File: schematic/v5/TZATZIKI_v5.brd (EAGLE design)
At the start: 41.1 x 50.1 mm, 21 parts, among them J1 2X20-CHIP-HEADERS2X20CHIP_OFF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, U2 DS2431P

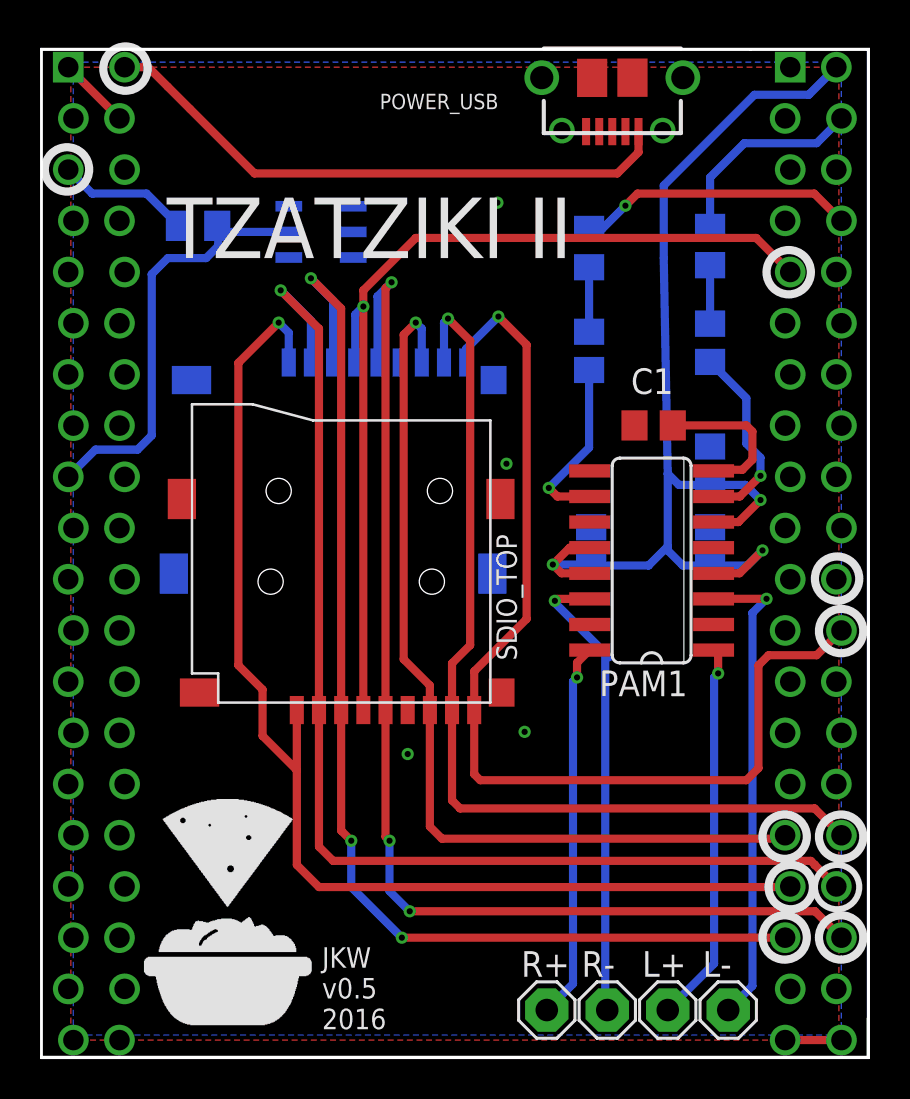
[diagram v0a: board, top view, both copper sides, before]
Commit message: connected audio gnd
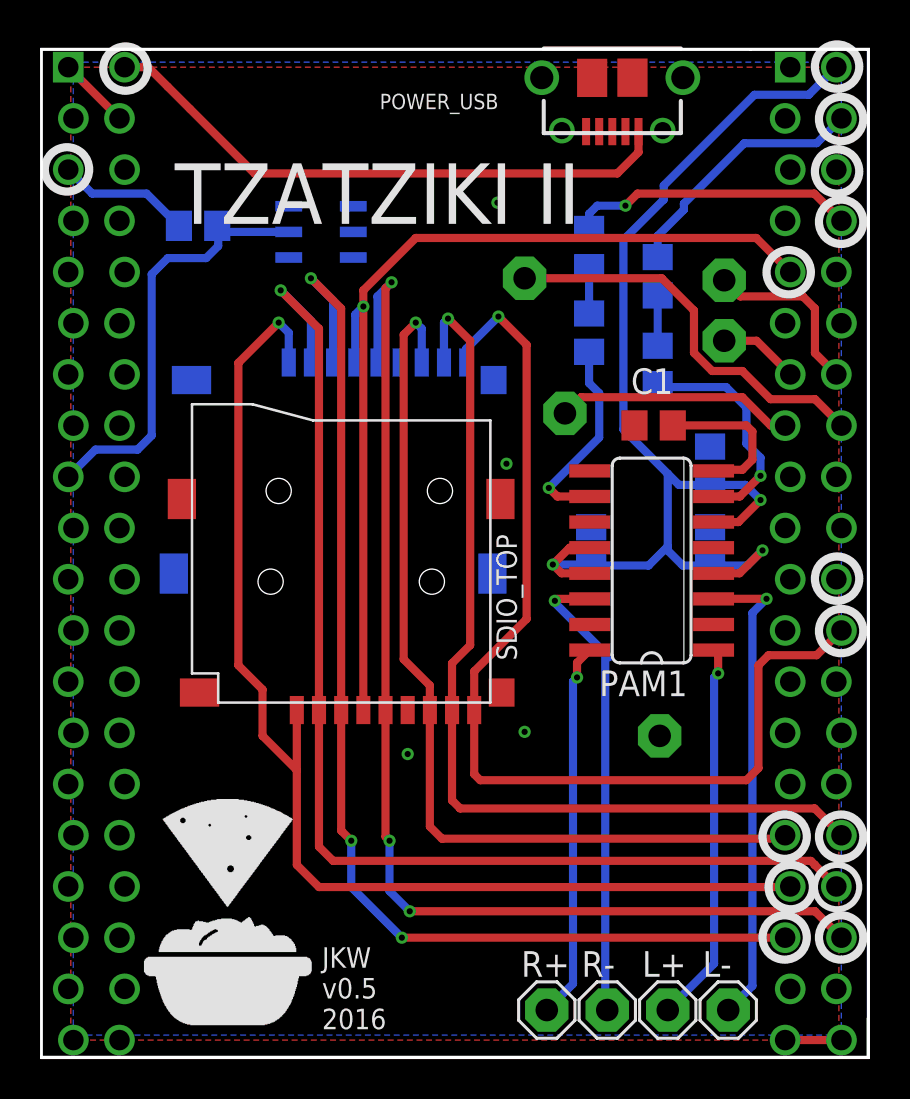
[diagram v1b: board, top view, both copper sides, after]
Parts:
- added GND, P0, P1, P3, P4: SE11, solpad:SE11
- moved R1 3.00 mm to (38.0, 54.4)
- moved C5 2.82 mm to (38.0, 50.0)
- moved C4 0.90 mm to (34.6, 51.6)
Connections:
- new net N$23: J1.XIO-P1, P1.MP
- new net N$24: J1.XIO-P3, P3.MP
- new net N$25: J1.XIO-P0, P0.MP
- new net N$26: J1.XIO-P2, P4.MP
- net GND: now also GND.MP, J1.HPCOM
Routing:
- net N$24: track 0.00 -> 20.0 mm
- net N$26: track 0.00 -> 11.8 mm
- net N$23: track 0.00 -> 8.79 mm
- net N$25: track 0.00 -> 3.97 mm
- net N$19: track 10.2 -> 12.8 mm
- net N$15: track 9.44 -> 11.3 mm
- net N$7: track 55.5 -> 57.3 mm
- net N$18: track 8.88 -> 10.2 mm
- net N$21: track 3.20 -> 2.30 mm

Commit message: added shutdown pin control
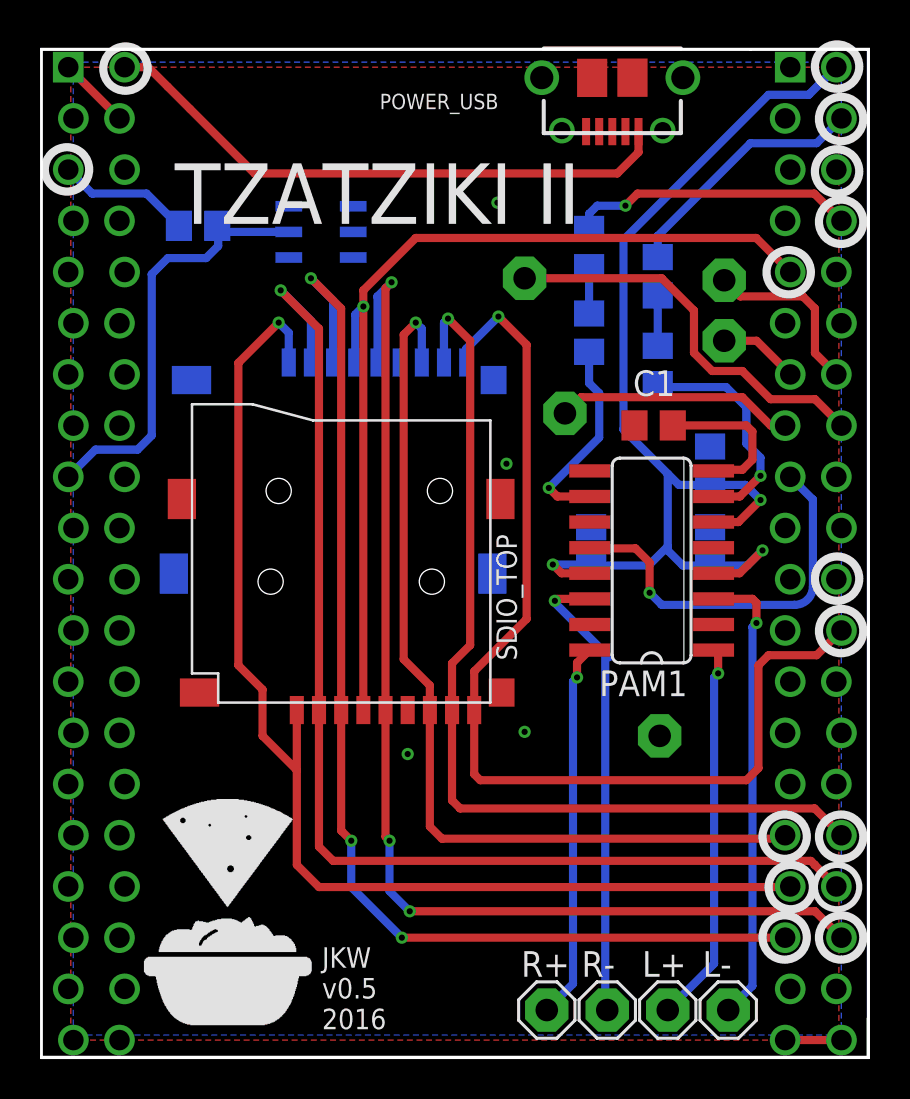
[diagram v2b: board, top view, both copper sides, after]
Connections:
- new net N$27: J1.XIO-P4, PAM1.12
- net N$7: no longer PAM1.12
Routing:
- net N$27: track 0.00 -> 19.4 mm, vias 0 -> 1
- net N$7: track 57.3 -> 54.7 mm
- net N$12: track 23.8 -> 23.0 mm

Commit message: added bat con and pwrbutton
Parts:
- added PWR-BTN, VBAT: (no value), pinhead:1X02
- moved U$2 8.99 mm to (31.6, 19.5)
- moved U$1 7.83 mm to (20.3, 17.9)
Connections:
- new net N$28: J1.BAT, VBAT.2
- new net N$29: J1.PWRON, PWR-BTN.2
- net GND: now also PWR-BTN.1, VBAT.1
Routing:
- net N$28: track 0.00 -> 38.5 mm
- net N$29: track 0.00 -> 27.7 mm
- net N$11: track 19.0 -> 21.9 mm
- net N$13: track 18.7 -> 19.5 mm
- net GND: vias 4 -> 5

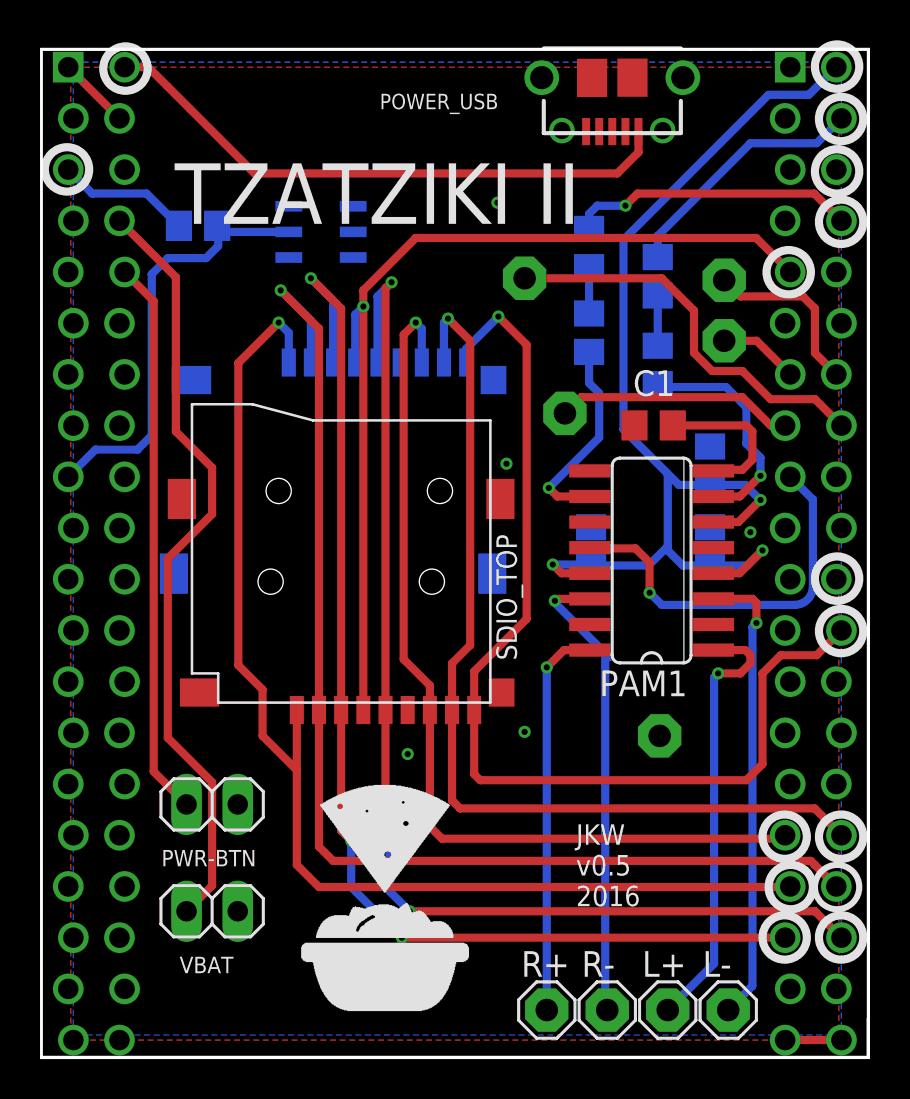
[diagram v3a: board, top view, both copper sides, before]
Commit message: added bat con and pwrbutton
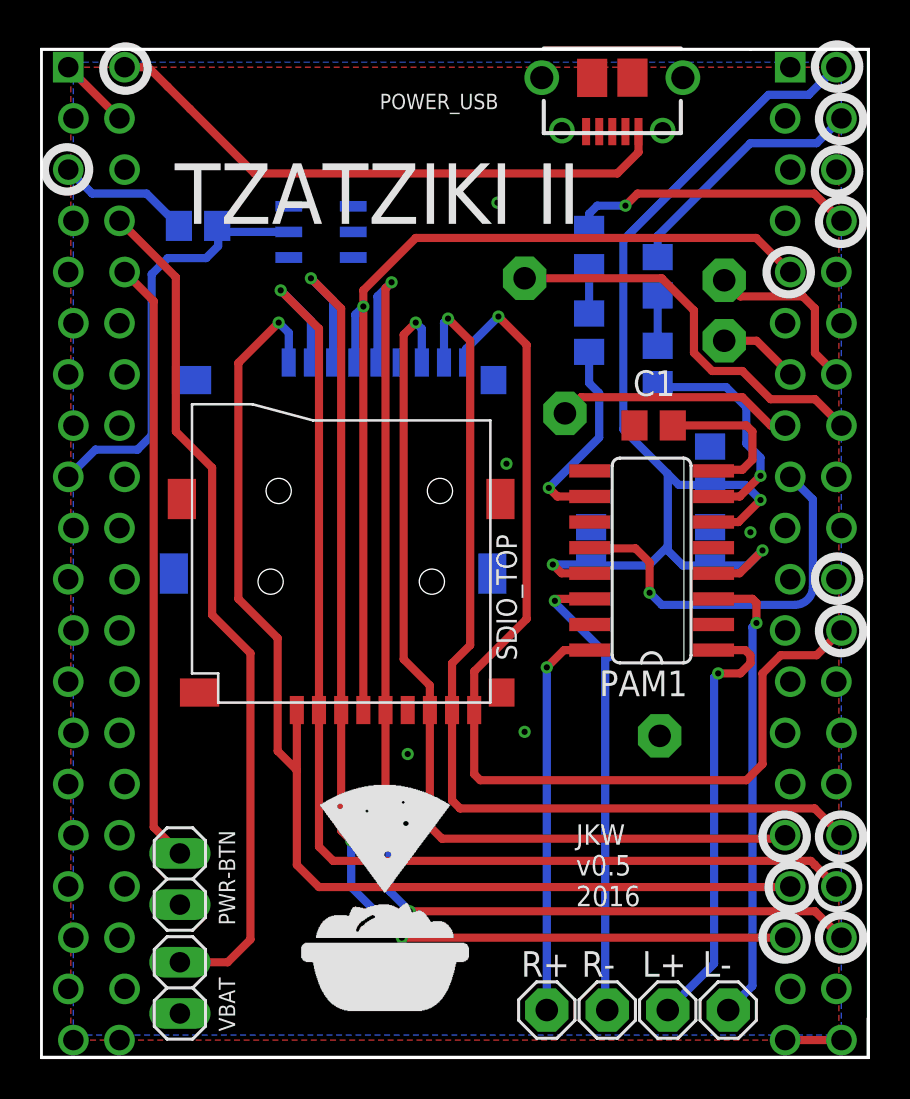
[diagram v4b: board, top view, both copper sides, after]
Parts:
- moved VBAT 4.12 mm to (14.3, 19.1), turned to 90 degrees
- moved PWR-BTN 4.03 mm to (14.3, 24.5), turned to 90 degrees
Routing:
- net N$28: track 38.5 -> 42.3 mm
- net N$29: track 27.7 -> 30.0 mm
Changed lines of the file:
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@@
 <element name="P4" library="solpad" package="SE11" value="SE11" x="33.4" y="47.6" rot="MR180"/>
 <element name="GND" library="solpad" package="SE11" value="SE11" x="38.1" y="31.6" rot="MR180"/>
-<element name="PWR-BTN" library="pinhead" package="1X02" value="" x="15.9" y="28.2" smashed="yes" rot="R180">
-<attribute name="NAME" x="13.3838" y="25.1288" size="0.8128" layer="25" ratio="10"/>
-<attribute name="VALUE" x="18.44" y="31.375" size="1.27" layer="27" rot="R180"/>
+<element name="PWR-BTN" library="pinhead" package="1X02" value="" x="14.3" y="24.5" smashed="yes" rot="R90">
+<attribute name="NAME" x="16.2288" y="26.9162" size="0.8128" layer="25" ratio="10" rot="R270"/>
+<attribute name="VALUE" x="17.475" y="21.96" size="1.27" layer="27" rot="R90"/>
 </element>
-<element name="VBAT" library="pinhead" package="1X02" value="" x="15.9" y="22.9" smashed="yes" rot="R180">
-<attribute name="NAME" x="14.2838" y="19.8288" size="0.8128" layer="25" ratio="10"/>
-<attribute name="VALUE" x="18.44" y="26.075" size="1.27" layer="27" rot="R180"/>
+<element name="VBAT" library="pinhead" package="1X02" value="" x="14.3" y="19.1" smashed="yes" rot="R90">
+<attribute name="NAME" x="16.2288" y="19.6162" size="0.8128" layer="25" ratio="10" rot="R270"/>
+<attribute name="VALUE" x="17.475" y="16.56" size="1.27" layer="27" rot="R90"/>
 </element>
 </elements>
@@
 <wire x1="19.2" y1="52.1" x2="19.7" y2="51.6" width="0.4064" layer="16"/>
 <wire x1="19.7" y1="51.6" x2="19.7" y2="50.12" width="0.4064" layer="16"/>
-<wire x1="17.2" y1="35.1" x2="17.2" y2="50.1" width="0.4064" layer="1"/>
 <wire x1="17.2" y1="50.1" x2="19.2" y2="52.1" width="0.4064" layer="1"/>
-<wire x1="17.2" y1="35.1" x2="18.4" y2="33.9" width="0.4064" layer="1"/>
-<wire x1="18.4" y1="33.9" x2="18.4" y2="31.6" width="0.4064" layer="1"/>
-<wire x1="18.4" y1="31.6" x2="20.1" y2="29.9" width="0.4064" layer="1"/>
+<wire x1="19.15" y1="30.85" x2="20.1" y2="29.9" width="0.4064" layer="1"/>
+<wire x1="17.2" y1="50.1" x2="17.2" y2="38.4" width="0.4064" layer="1"/>
+<wire x1="17.2" y1="38.4" x2="19.15" y2="36.45" width="0.4064" layer="1"/>
+<wire x1="19.15" y1="36.45" x2="19.15" y2="30.85" width="0.4064" layer="1"/>
 </signal>
 <signal name="N$5">
@@
 <wire x1="14.1" y1="54.353" x2="14.1" y2="46.7" width="0.4064" layer="1"/>
 <wire x1="14.1" y1="46.7" x2="15.9" y2="44.9" width="0.4064" layer="1"/>
-<wire x1="15.9" y1="44.9" x2="15.9" y2="42.6" width="0.4064" layer="1"/>
-<wire x1="15.9" y1="42.6" x2="13.7" y2="40.4" width="0.4064" layer="1"/>
-<wire x1="13.7" y1="40.4" x2="13.7" y2="31.5" width="0.4064" layer="1"/>
-<wire x1="13.7" y1="31.5" x2="15.9" y2="29.3" width="0.4064" layer="1"/>
-<wire x1="15.9" y1="29.3" x2="15.9" y2="24.17" width="0.4064" layer="1"/>
-<wire x1="15.9" y1="24.17" x2="14.63" y2="22.9" width="0.4064" layer="1"/>
+<wire x1="15.9" y1="44.9" x2="15.9" y2="37.6" width="0.4064" layer="1"/>
+<wire x1="15.9" y1="37.6" x2="17.8" y2="35.7" width="0.4064" layer="1"/>
+<wire x1="17.8" y1="35.7" x2="17.8" y2="21.5" width="0.4064" layer="1"/>
+<wire x1="17.8" y1="21.5" x2="16.67" y2="20.37" width="0.4064" layer="1"/>
+<wire x1="16.67" y1="20.37" x2="14.3" y2="20.37" width="0.4064" layer="1"/>
 </signal>
 <signal name="N$29">
@@
 <contactref element="PWR-BTN" pad="2"/>
 <wire x1="11.557" y1="54.61" x2="13" y2="53.167" width="0.4064" layer="1"/>
-<wire x1="13" y1="53.167" x2="13" y2="29.83" width="0.4064" layer="1"/>
-<wire x1="13" y1="29.83" x2="14.63" y2="28.2" width="0.4064" layer="1"/>
+<wire x1="13" y1="53.167" x2="13" y2="27.07" width="0.4064" layer="1"/>
+<wire x1="13" y1="27.07" x2="14.3" y2="25.77" width="0.4064" layer="1"/>
 </signal>
 </signals>

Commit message: rotated connector for free passage of the SD card
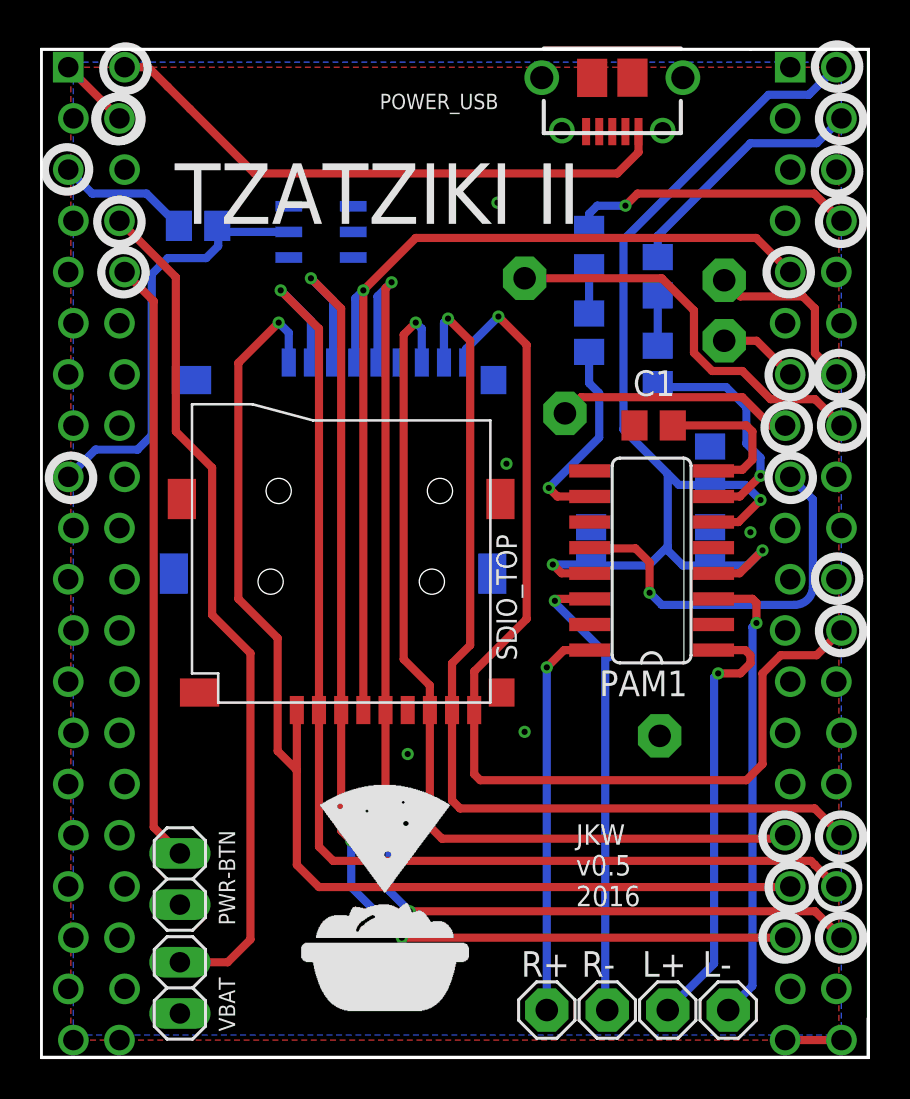
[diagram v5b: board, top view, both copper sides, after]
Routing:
- net N$10: track 46.7 -> 47.5 mm
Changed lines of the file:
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@@
 <circle x="46.9" y="59.7" radius="1.1" width="0.4064" layer="26"/>
 <circle x="46.9" y="59.6" radius="1.1" width="0.4064" layer="25"/>
+<circle x="11.3" y="57.1" radius="1.1" width="0.4064" layer="25"/>
+<circle x="11.5" y="54.6" radius="1.1" width="0.4064" layer="25"/>
+<circle x="8.9" y="44.4" radius="1.1" width="0.4064" layer="25"/>
+<circle x="47.2" y="47" radius="1.1" width="0.4064" layer="25"/>
+<circle x="47" y="49.5" radius="1.1" width="0.4064" layer="25"/>
+<circle x="44.6" y="49.5" radius="1.1" width="0.4064" layer="25"/>
+<circle x="44.4" y="46.9" radius="1.1" width="0.4064" layer="25"/>
+<circle x="44.6" y="44.4" radius="1.1" width="0.4064" layer="25"/>
+<circle x="11.3" y="62.2" radius="1.1" width="0.4064" layer="25"/>
+<circle x="11.2" y="62.2" radius="1.1" width="0.4064" layer="25"/>
+<circle x="11.3" y="62.2" radius="1.1" width="0.4064" layer="26"/>
+<circle x="11.3" y="57.1" radius="1.1" width="0.4064" layer="26"/>
+<circle x="11.6" y="54.6" radius="1.1" width="0.4064" layer="26"/>
+<circle x="8.8" y="44.5" radius="1.1" width="0.4064" layer="26"/>
+<circle x="44.6" y="44.4" radius="1.1" width="0.4064" layer="26"/>
+<circle x="44.3" y="47" radius="1.1" width="0.4064" layer="26"/>
+<circle x="44.6" y="49.5" radius="1.1" width="0.4064" layer="26"/>
+<circle x="46.9" y="49.5" radius="1.1" width="0.4064" layer="26"/>
+<circle x="47.1" y="47" radius="1.1" width="0.4064" layer="26"/>
 </plain>
 <attributes>
@@
 <contactref element="SDIO_BOT" pad="4"/>
 <contactref element="SDIO_TOP" pad="4"/>
-<wire x1="23.4" y1="32.88" x2="23.4" y2="52.9" width="0.4064" layer="1"/>
-<wire x1="23.4" y1="52.9" x2="23.4" y2="53.7" width="0.4064" layer="1"/>
-<wire x1="23" y1="50.12" x2="23" y2="52.5" width="0.4064" layer="16"/>
-<wire x1="23" y1="52.5" x2="23.4" y2="52.9" width="0.4064" layer="16"/>
-<via x="23.4" y="52.9" extent="1-16" drill="0.3048"/>
+<wire x1="23.4" y1="32.88" x2="23.4" y2="53.7" width="0.4064" layer="1"/>
+<wire x1="23" y1="50.12" x2="23" y2="53.3" width="0.4064" layer="16"/>
+<wire x1="23" y1="53.3" x2="23.4" y2="53.7" width="0.4064" layer="16"/>
+<via x="23.4" y="53.7" extent="1-16" drill="0.3048"/>
 <wire x1="44.577" y1="54.61" x2="42.887" y2="56.3" width="0.4064" layer="1"/>
 <wire x1="42.887" y1="56.3" x2="26" y2="56.3" width="0.4064" layer="1"/>
